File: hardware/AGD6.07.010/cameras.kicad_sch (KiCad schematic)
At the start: 0 parts

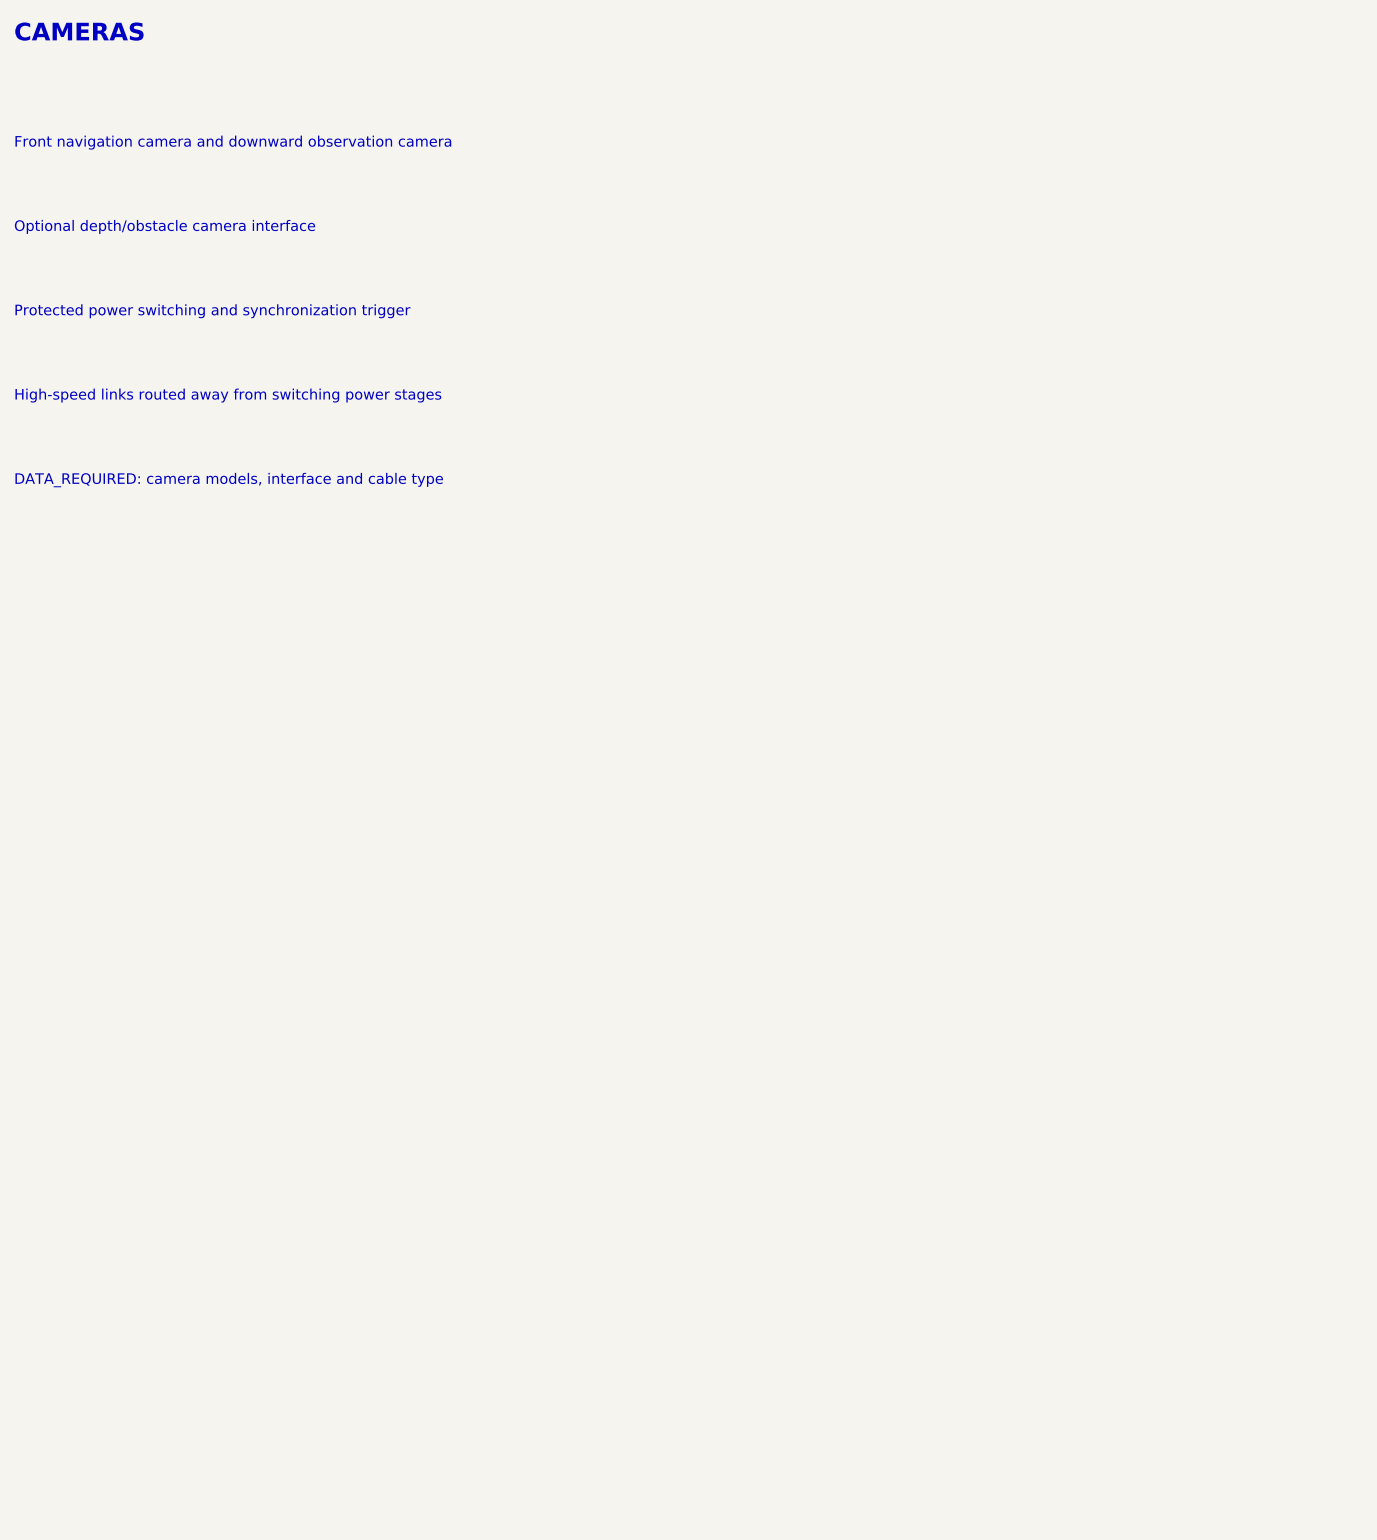
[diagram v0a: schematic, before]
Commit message: Draw full AGD6.07.010 schematic per integrated_avionics_board spec
All ten sheets now carry components: 14S input with hot-swap and power
monitor, 12/5/3.3 V rails and a separate 12 V AI channel with soft-start
and current telemetry, Pixhawk connectors, CAN1/CAN2 hub with chokes,
ESD and switchable termination, sensor conditioning, SIYI and radar,
AI interface and watchdog, protected 12 V switches with diagnostics,
fan/heater control, cameras and Ethernet. Open choices are recorded in
DECISIONS.md; datasheet-dependent values are flagged CHECK_DATASHEET.

ERC: no errors. All 752 intended pin connections match the KiCad netlist.

Co-Authored-By: Claude Opus 5.5 <noreply@anthropic.com>
Claude-Session: https://claude.ai/code/session_01Qk7uTKdi6YbndB9fGuguYV
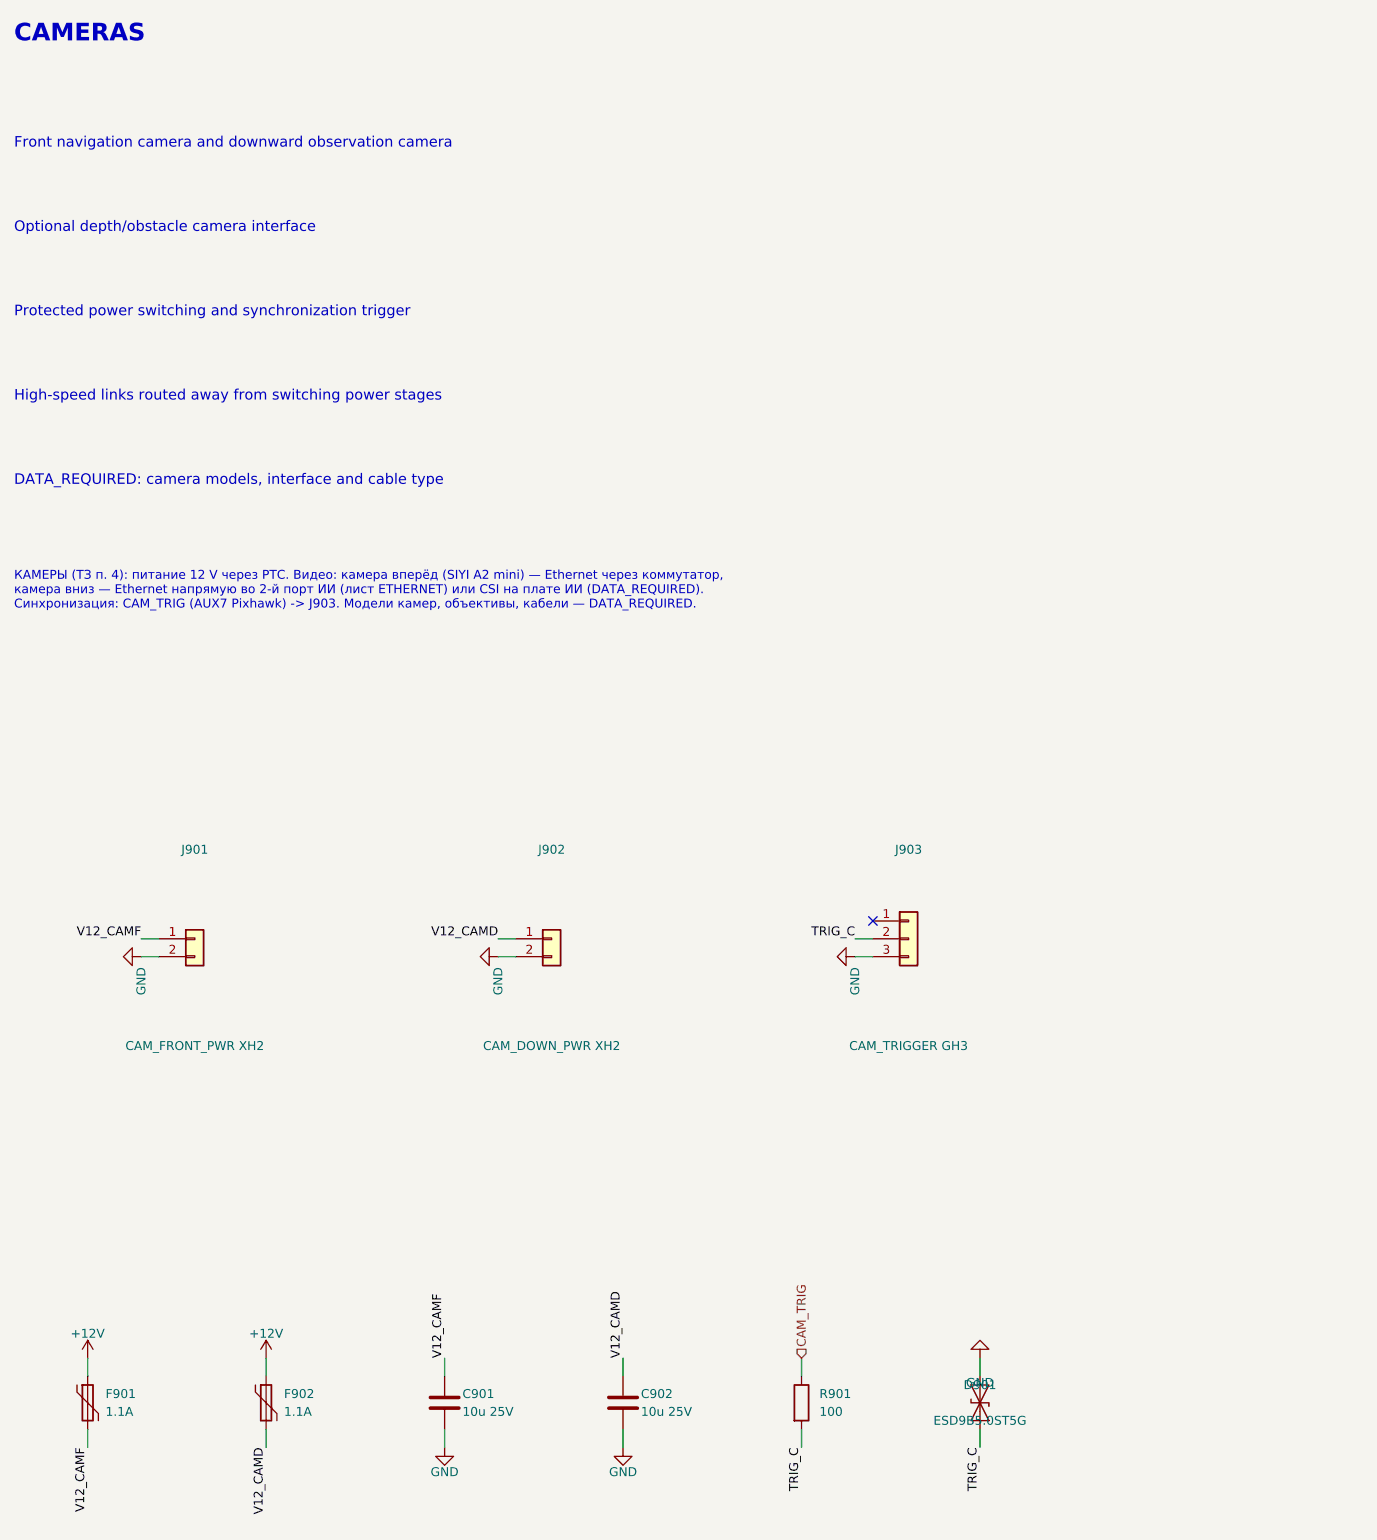
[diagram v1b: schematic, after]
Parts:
- added C901, C902: 10u 25V, Capacitor_SMD:C_1210_3225Metric, symbol Device:C
- added D901: ESD9B5.0ST5G, Diode_SMD:D_SOD-923, symbol Diode:ESD9B5.0ST5G
- added F901, F902: 1.1A, Fuse:Fuse_1812_4532Metric, symbol Device:Polyfuse
- added J901: CAM_FRONT_PWR XH2, Connector_JST:JST_XH_B2B-XH-A_1x02_P2.50mm_Vertical, symbol Connector_Generic:Conn_01x02
- added J902: CAM_DOWN_PWR XH2, Connector_JST:JST_XH_B2B-XH-A_1x02_P2.50mm_Vertical, symbol Connector_Generic:Conn_01x02
- added J903: CAM_TRIGGER GH3, Connector_JST:JST_GH_SM03B-GHS-TB_1x03-1MP_P1.25mm_Horizontal, symbol Connector_Generic:Conn_01x03
- added R901: 100, Resistor_SMD:R_0402_1005Metric, symbol Device:R
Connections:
- new net +12V: F901.1, F902.1
- new net CAM_TRIG: R901.1
- new net GND: C901.2, C902.2, D901.2 (A2), J901.2 (Pin_2), J902.2 (Pin_2), J903.3 (Pin_3)
- new net TRIG_C: D901.1 (A1), J903.2 (Pin_2), R901.2
- new net V12_CAMD: C902.1, F902.2, J902.1 (Pin_1)
- new net V12_CAMF: C901.1, F901.2, J901.1 (Pin_1)
- no-connect marks 0 -> 1
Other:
- note added: "КАМЕРЫ (ТЗ п. 4): питание 12 V через PTC. Видео: камера вперёд (SIYI A2 mini) — Ethernet через коммутатор, камера вниз — Ethernet напрямую во 2-й порт ИИ (лист ETHERNET) или CSI на плате ИИ (DATA_REQUIRED). Синхронизация: CAM_TRIG (AUX7 Pixhawk) -> J903. Модели камер, объективы, кабели — DATA_REQUIRED."
- company: (none) -> АГД6.07.010
- title: (none) -> CAMERAS
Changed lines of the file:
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@@
-(kicad_sch
-	(version 20260306)
-	(generator "eeschema")
-	(generator_version "10.0")
-	(paper "A4")
-	(text "Protected power switching and synchronization trigger"
-		(exclude_from_sim no)
-		(at 20 59 0)
-		(effects
-			(font
-				(size 1.5 1.5)
-			)
-			(justify left bottom)
-		)
-	)
-	(text "CAMERAS"
-		(exclude_from_sim no)
-		(at 20 20 0)
-		(effects
-			(font
-				(size 2.5 2.5)
-				(bold yes)
-			)
-			(justify left bottom)
-		)
-	)
-	(text "High-speed links routed away from switching power stages"
-		(exclude_from_sim no)
-		(at 20 71 0)
-		(effects
-			(font
-				(size 1.5 1.5)
-			)
-			(justify left bottom)
-		)
-	)
-	(text "Front navigation camera and downward observation camera"
-		(exclude_from_sim no)
-		(at 20 35 0)
-		(effects
-			(font
-				(size 1.5 1.5)
-			)
-			(justify left bottom)
-		)
-	)
-	(text "Optional depth/obstacle camera interface"
-		(exclude_from_sim no)
-		(at 20 47 0)
-		(effects
-			(font
-				(size 1.5 1.5)
-			)
-			(justify left bottom)
-		)
-	)
-	(text "DATA_REQUIRED: camera models, interface and cable type"
-		(exclude_from_sim no)
-		(at 20 83 0)
-		(effects
-			(font
-				(size 1.5 1.5)
-			)
-			(justify left bottom)
-		)
-	)
-	(sheet_instances
-		(path "/"
-			(page "1")
-		)
-	)
-)

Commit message: AGD6.07.010 rev 0.3: design review fixes and bring-up plan
Design review (DESIGN_REVIEW.md) with fixes applied to the schematic:
INA228 input RC filters, 12 V bus current monitor (INA228 0x45),
BTS5030 diagnostic scaling with clamp diodes, flow input level fix,
CAN1 changed from star to daisy chain with on-board terminator, AI
shutdown request, board buzzer, series resistors and ESD on external
I2C probes. Connectors merged so every connector sits on a board edge.
Adds calculations.md (power, IPC-2221 widths, hot-swap, thermal, ADC
scaling, CAN, clearances) and BRINGUP.md (step-by-step test plan).
ERC: no errors; all 820 intended pin connections verified. Board is
re-placed; routing in progress.

Co-Authored-By: Claude Opus 5.5 <noreply@anthropic.com>
Claude-Session: https://claude.ai/code/session_01Qk7uTKdi6YbndB9fGuguYV
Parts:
- removed D901: ESD9B5.0ST5G, Diode_SMD:D_SOD-923, symbol Diode:ESD9B5.0ST5G
- removed J903: CAM_TRIGGER GH3, Connector_JST:JST_GH_SM03B-GHS-TB_1x03-1MP_P1.25mm_Horizontal, symbol Connector_Generic:Conn_01x03
- removed R901: 100, Resistor_SMD:R_0402_1005Metric, symbol Device:R
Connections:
- no-connect marks 1 -> 0
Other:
- note added: "КАМЕРЫ (ТЗ п. 4): питание 12 V через PTC. Видео: камера вперёд (SIYI A2 mini) — Ethernet через коммутатор, камера вниз — Ethernet напрямую во 2-й порт ИИ (лист ETHERNET) или CSI на плате ИИ (DATA_REQUIRED). Синхронизация: CAM_TRIG (AUX7 Pixhawk) -> J806 на листе LOAD_SWITCHES_12V. Модели камер, объективы, кабели — DATA_REQUIRED."
- note removed: "КАМЕРЫ (ТЗ п. 4): питание 12 V через PTC. Видео: камера вперёд (SIYI A2 mini) — Ethernet через коммутатор, камера вниз — Ethernet напрямую во 2-й порт ИИ (лист ETHERNET) или CSI на плате ИИ (DATA_REQUIRED). Синхронизация: CAM_TRIG (AUX7 Pixhawk) -> J903. Модели камер, объективы, кабели — DATA_REQUIRED."

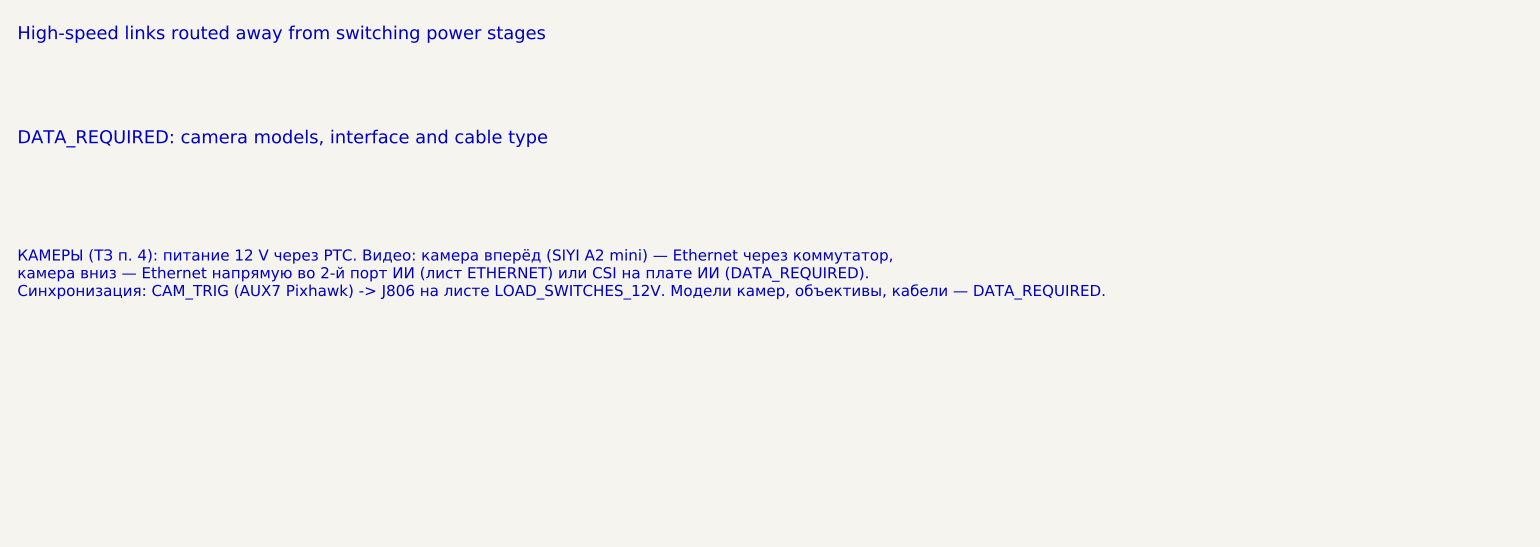
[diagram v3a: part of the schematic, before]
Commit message: AGD6.07.010 rev 0.4 (WIP): 3x TRACO THL40 DC/DC, split 12 V bus, SwitchBlox Ethernet, fixed LM5069 UVLO/OVLO, computed hot-swap values, PX4 firmware notes; board re-placed, routing in progress
Co-Authored-By: Claude Opus 5.5 <noreply@anthropic.com>
Claude-Session: https://claude.ai/code/session_01Qk7uTKdi6YbndB9fGuguYV
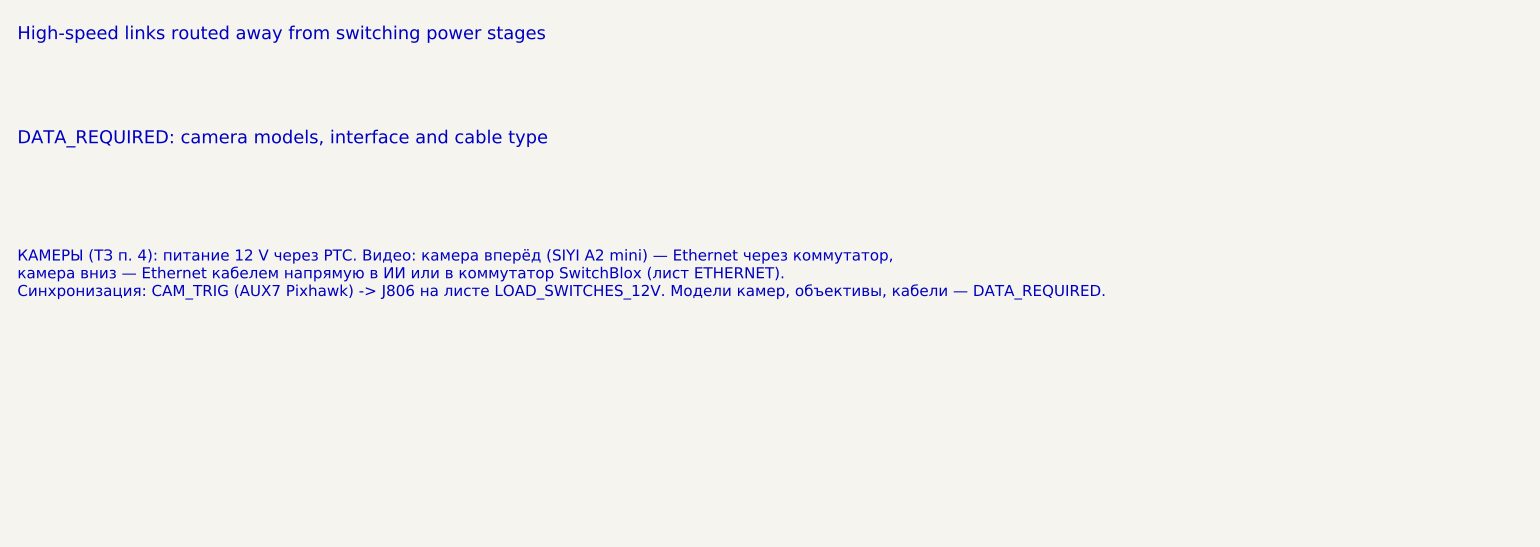
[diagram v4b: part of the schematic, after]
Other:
- note added: "КАМЕРЫ (ТЗ п. 4): питание 12 V через PTC. Видео: камера вперёд (SIYI A2 mini) — Ethernet через коммутатор, камера вниз — Ethernet кабелем напрямую в ИИ или в коммутатор SwitchBlox (лист ETHERNET). Синхронизация: CAM_TRIG (AUX7 Pixhawk) -> J806 на листе LOAD_SWITCHES_12V. Модели камер, объективы, кабели — DATA_REQUIRED."
- note removed: "КАМЕРЫ (ТЗ п. 4): питание 12 V через PTC. Видео: камера вперёд (SIYI A2 mini) — Ethernet через коммутатор, камера вниз — Ethernet напрямую во 2-й порт ИИ (лист ETHERNET) или CSI на плате ИИ (DATA_REQUIRED). Синхронизация: CAM_TRIG (AUX7 Pixhawk) -> J806 на листе LOAD_SWITCHES_12V. Модели камер, объективы, кабели — DATA_REQUIRED."
